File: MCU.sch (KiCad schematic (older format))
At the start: 27 parts, among them J801 TEST_2P, P801 JTAG, U801 STM32F756VGTx, Y801 32kHz, Y802 24MHz

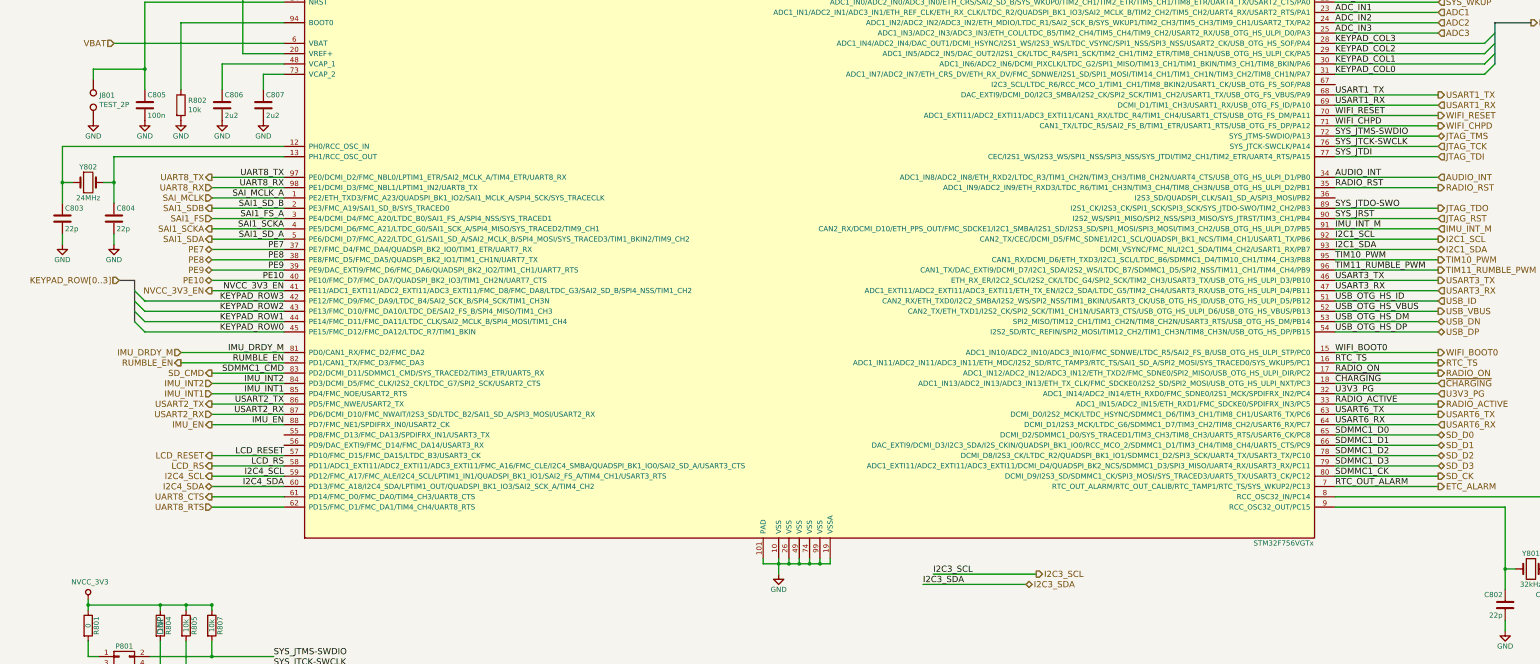
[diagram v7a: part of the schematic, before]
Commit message: fix for several signals
* some signals where not routed out to the top sheet.
* I2C signals where not connected.
* moved imu subsheet to the other side of the mcu sheet to
  share I2C bus with audio
* changed footprint of crystals to crystals I have
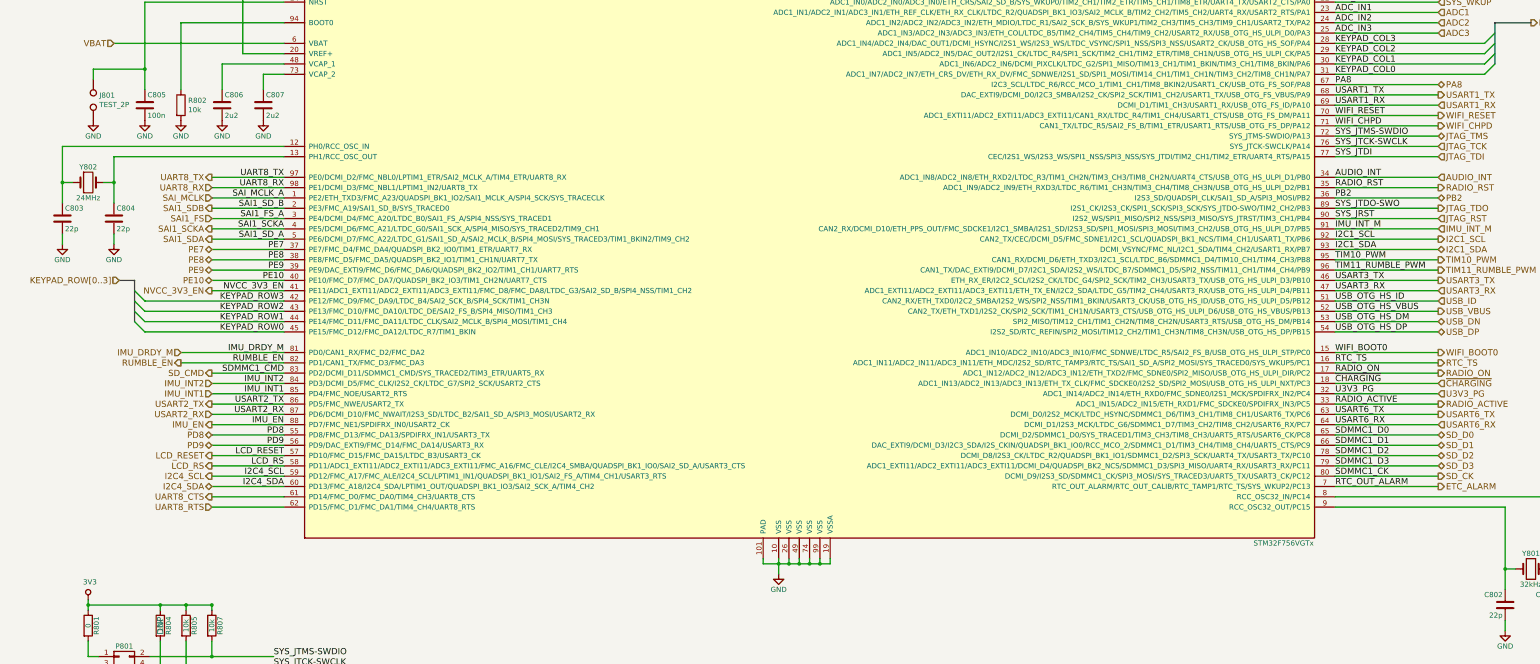
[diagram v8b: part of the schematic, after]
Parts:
- Y801: footprint Crystals:Crystal_SMD_SeikoEpson_MC146-4pin_6.7x1.5mm_HandSoldering -> Crystals:Crystal_SMD_2012-2pin_2.0x1.2mm
- Y802: footprint Crystals:Crystal_SMD_SeikoEpson_MC146-4pin_6.7x1.5mm_HandSoldering -> Crystals:Crystal_SMD_2016-4pin_2.0x1.6mm
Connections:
- net NVCC_3V3 is gone; now on net 3V3: R801.1, R804.1, R805.1, R807.1
- net PB2: now reaches U801.36 (I2S3_SD/QUADSPI_CLK/SAI1_SD_A/SPI3_MOSI/PB2)
- net PD8: now reaches U801.55 (PD8/FMC_D13/FMC_DA13/SPDIFRX_IN1/USART3_TX)
- net PD9: now reaches U801.56 (PD9/DAC_EXTI9/FMC_D14/FMC_DA14/USART3_RX)
- net PA8: now reaches U801.67 (I2C3_SCL/LTDC_R6/RCC_MCO_1/TIM1_CH1/TIM8_BKIN2/USART1_CK/USB_OTG_FS_SOF/PA8)
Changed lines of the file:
@@
 F 0 "Y802" H 1050 4900 50  0000 C CNN
 F 1 "24MHz" H 1050 4600 50  0000 C CNN
-F 2 "Crystals:Crystal_SMD_SeikoEpson_MC146-4pin_6.7x1.5mm_HandSoldering" H 1050 4750 50  0001 C CNN
+F 2 "Crystals:Crystal_SMD_2016-4pin_2.0x1.6mm" H 1050 4750 50  0001 C CNN
 F 3 "" H 1050 4750 50  0000 C CNN
 	1    1050 4750
@@
 F 0 "Y801" H 15050 8650 50  0000 C CNN
 F 1 "32kHz" H 15050 8350 50  0000 C CNN
-F 2 "Crystals:Crystal_SMD_SeikoEpson_MC146-4pin_6.7x1.5mm_HandSoldering" H 15050 8500 50  0001 C CNN
+F 2 "Crystals:Crystal_SMD_2012-2pin_2.0x1.2mm" H 15050 8500 50  0001 C CNN
 F 3 "" H 15050 8500 50  0000 C CNN
 	1    15050 8500
@@
 Text Label 13150 7200 0    60   ~ 0
 SDMMC1_D0
-Text Label 9150 8650 0    60   ~ 0
-I2C3_SDA
-Text Label 9250 8550 0    60   ~ 0
-I2C3_SCL
 Text Label 13150 4300 0    60   ~ 0
 SYS_JTMS-SWDIO
@@
 Text HLabel 14150 3300 2    60   Input ~ 0
 ADC3
-Text HLabel 10250 8550 2    60   Output ~ 0
-I2C3_SCL
 Text HLabel 14150 3900 2    60   Output ~ 0
 USART1_TX
@@
 Text HLabel 14150 7200 2    60   BiDi ~ 0
 SD_D0
-Text HLabel 10150 8650 2    60   BiDi ~ 0
-I2C3_SDA
 Text HLabel 14150 7600 2    60   Output ~ 0
 SD_CK
@@
 	13150 3300 14150 3300
 Wire Wire Line
-	9250 8550 10250 8550
-Wire Wire Line
 	13150 3900 14150 3900
 Wire Wire Line
@@
 Wire Wire Line
 	13150 7200 14150 7200
-Wire Wire Line
-	9150 8650 10150 8650
 Wire Wire Line
 	13150 7600 14150 7600
@@
 	7600 8450 7600 8400
 $Comp
-L NVCC_3V3 #PWR019
-U 1 1 59B56807
+L 3V3 #PWR0808
+U 1 1 59BABD47
 P 1050 8800
-F 0 "#PWR019" H 1050 8650 50  0001 C CNN
-F 1 "NVCC_3V3" H 1067 8973 50  0000 C CNN
+F 0 "#PWR0808" H 1050 8650 50  0001 C CNN
+F 1 "3V3" H 1067 8973 50  0000 C CNN
 F 2 "" H 1050 8800 50  0001 C CNN
 F 3 "" H 1050 8800 50  0001 C CNN
@@
 	1    0    0    -1
 $EndComp
+Text Label 2950 7200 2    60   ~ 0
+PD8
+Text HLabel 2250 7200 0    60   BiDi ~ 0
+PD8
+Wire Wire Line
+	2250 7200 2950 7200
+Text Label 2950 7300 2    60   ~ 0
+PD9
+Text HLabel 2250 7300 0    60   BiDi ~ 0
+PD9
+Wire Wire Line
+	2250 7300 2950 7300
+Text Label 13150 4900 0    60   ~ 0
+PB2
+Text HLabel 14150 4900 2    60   BiDi ~ 0
+PB2
+Wire Wire Line
+	13150 4900 14150 4900
+Text Label 13150 3800 0    60   ~ 0
+PA8
+Text HLabel 14150 3800 2    60   BiDi ~ 0
+PA8
+Wire Wire Line
+	13150 3800 14150 3800
 $EndSCHEMATC
